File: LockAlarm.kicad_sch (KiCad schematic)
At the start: 6 parts, among them SW1 Reed Switch

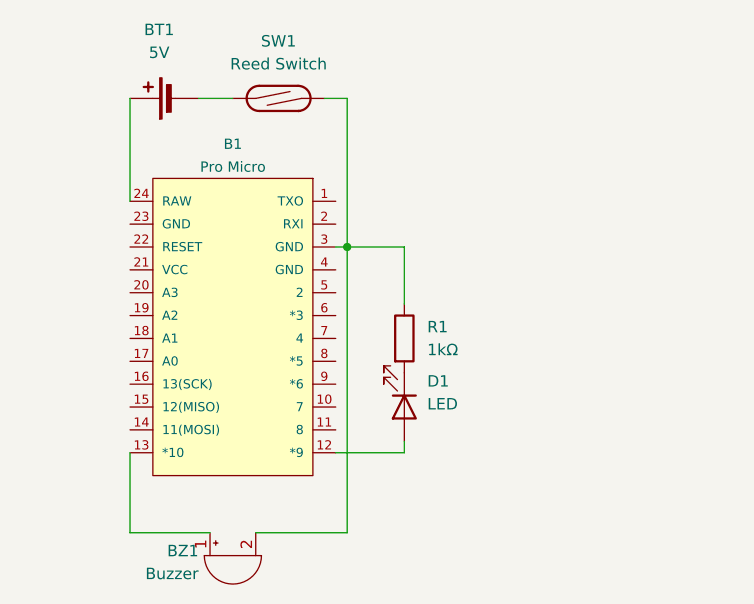
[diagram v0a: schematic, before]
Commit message: Replace ProMicro with ATtiny13A-P
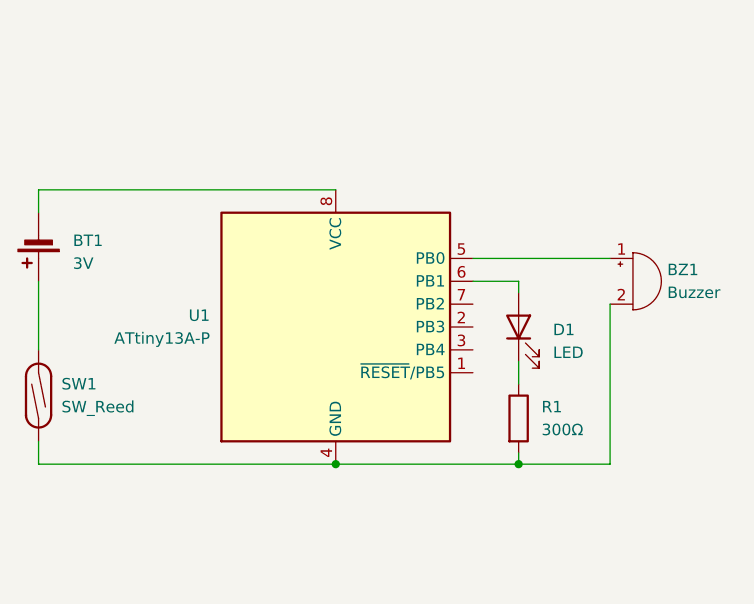
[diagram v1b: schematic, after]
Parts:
- removed B1: Pro Micro, SPARKFUN_PRO_MICRO, symbol SparkFun-Boards:SPARKFUN_PRO_MICRO
- added U1: ATtiny13A-P, Package_DIP:DIP-8_W7.62mm, symbol MCU_Microchip_ATtiny:ATtiny13A-P
- BT1: value 5V -> 3V
- R1: value 1kΩ -> 300Ω
- SW1: value Reed Switch -> SW_Reed
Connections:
- net at BT1.1 (+): now also SW1.1
- net at BT1.2 (-): now also U1.8 (VCC); no longer SW1.1
- net at BZ1.1 (-): now also U1.5 (PB0)
- net at BZ1.2 (+), SW1.2: now also R1.2, U1.4 (GND); no longer R1.1
- net at D1.1 (K): now also R1.1; no longer R1.2
- net at D1.2 (A): now also U1.6 (PB1)
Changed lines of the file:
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@@
 (kicad_sch (version 20230121) (generator eeschema)
   (paper "A5")
-  (junction (at 110.49 52.07) (diameter 0) (color 0 0 0 0)
+  (junction (at 109.22 76.2) (diameter 0) (color 0 0 0 0)
   )
-  (wire (pts (xy 86.36 83.82) (xy 95.25 83.82))
+  (junction (at 129.54 76.2) (diameter 0) (color 0 0 0 0)
+  )
+  (wire (pts (xy 129.54 76.2) (xy 139.7 76.2))
     (stroke (width 0) (type default))
   )
-  (wire (pts (xy 100.33 83.82) (xy 110.49 83.82))
+  (wire (pts (xy 124.46 53.34) (xy 139.7 53.34))
     (stroke (width 0) (type default))
   )
-  (wire (pts (xy 110.49 52.07) (xy 116.84 52.07))
+  (wire (pts (xy 76.2 45.72) (xy 76.2 48.26))
     (stroke (width 0) (type default))
   )
-  (wire (pts (xy 86.36 74.93) (xy 86.36 83.82))
+  (wire (pts (xy 129.54 55.88) (xy 124.46 55.88))
     (stroke (width 0) (type default))
   )
-  (wire (pts (xy 109.22 52.07) (xy 110.49 52.07))
+  (wire (pts (xy 109.22 76.2) (xy 129.54 76.2))
     (stroke (width 0) (type default))
   )
-  (wire (pts (xy 116.84 74.93) (xy 109.22 74.93))
+  (wire (pts (xy 129.54 67.31) (xy 129.54 64.77))
     (stroke (width 0) (type default))
   )
-  (wire (pts (xy 110.49 35.56) (xy 107.95 35.56))
+  (wire (pts (xy 109.22 45.72) (xy 76.2 45.72))
     (stroke (width 0) (type default))
   )
-  (wire (pts (xy 116.84 74.93) (xy 116.84 73.66))
+  (wire (pts (xy 76.2 76.2) (xy 109.22 76.2))
     (stroke (width 0) (type default))
   )
-  (wire (pts (xy 116.84 58.42) (xy 116.84 52.07))
+  (wire (pts (xy 129.54 57.15) (xy 129.54 55.88))
     (stroke (width 0) (type default))
   )
-  (wire (pts (xy 93.98 35.56) (xy 97.79 35.56))
+  (wire (pts (xy 139.7 58.42) (xy 139.7 76.2))
     (stroke (width 0) (type default))
   )
-  (wire (pts (xy 110.49 83.82) (xy 110.49 52.07))
+  (wire (pts (xy 129.54 74.93) (xy 129.54 76.2))
     (stroke (width 0) (type default))
   )
-  (wire (pts (xy 86.36 46.99) (xy 86.36 35.56))
+  (wire (pts (xy 76.2 73.66) (xy 76.2 76.2))
     (stroke (width 0) (type default))
   )
-  (wire (pts (xy 110.49 35.56) (xy 110.49 52.07))
+  (wire (pts (xy 76.2 55.88) (xy 76.2 63.5))
     (stroke (width 0) (type default))
   )
-  (symbol (lib_id "Device:Battery_Cell") (at 91.44 35.56 90) (unit 1)
+  (symbol (lib_id "Device:Buzzer") (at 142.24 55.88 0) (unit 1)
     (in_bom yes) (on_board yes) (dnp no) (fields_autoplaced)
-    (property "Reference" "BT1" (at 89.5985 27.94 90)
-      (effects (font (size 1.27 1.27)))
+    (property "Reference" "BZ1" (at 146.05 54.61 0)
+      (effects (font (size 1.27 1.27)) (justify left))
     )
-    (property "Value" "5V" (at 89.5985 30.48 90)
-      (effects (font (size 1.27 1.27)))
+    (property "Value" "Buzzer" (at 146.05 57.15 0)
+      (effects (font (size 1.27 1.27)) (justify left))
     )
-    (property "Footprint" "" (at 89.916 35.56 90)
+    (property "Footprint" "" (at 141.605 53.34 90)
       (effects (font (size 1.27 1.27)) hide)
     )
-    (property "Datasheet" "~" (at 89.916 35.56 90)
+    (property "Datasheet" "~" (at 141.605 53.34 90)
+      (effects (font (size 1.27 1.27)) hide)
+    )
+    (pin "1")
+    (pin "2")
+    (instances
+      (project "LockAlarm"
+        (path "/bfb8881f-b332-475f-bf27-97a988c7f65e"
+          (reference "BZ1") (unit 1)
+        )
+      )
+    )
+  )
+  (symbol (lib_id "Device:Battery_Cell") (at 76.2 50.8 180) (unit 1)
+    (in_bom yes) (on_board yes) (dnp no) (fields_autoplaced)
+    (property "Reference" "BT1" (at 80.01 51.3715 0)
+      (effects (font (size 1.27 1.27)) (justify right))
+    )
+    (property "Value" "3V" (at 80.01 53.9115 0)
+      (effects (font (size 1.27 1.27)) (justify right))
+    )
+    (property "Footprint" "" (at 76.2 52.324 90)
+      (effects (font (size 1.27 1.27)) hide)
+    )
+    (property "Datasheet" "~" (at 76.2 52.324 90)
       (effects (font (size 1.27 1.27)) hide)
     )
@@
     )
   )
-  (symbol (lib_id "Device:Buzzer") (at 97.79 86.36 90) (mirror x) (unit 1)
-    (in_bom yes) (on_board yes) (dnp no)
-    (property "Reference" "BZ1" (at 93.98 85.8451 90)
+  (symbol (lib_id "Switch:SW_Reed") (at 76.2 68.58 270) (unit 1)
+    (in_bom yes) (on_board yes) (dnp no) (fields_autoplaced)
+    (property "Reference" "SW1" (at 78.74 67.31 90)
       (effects (font (size 1.27 1.27)) (justify left))
     )
-    (property "Value" "Buzzer" (at 93.98 88.3851 90)
+    (property "Value" "SW_Reed" (at 78.74 69.85 90)
       (effects (font (size 1.27 1.27)) (justify left))
     )
-    (property "Footprint" "" (at 95.25 85.725 90)
+    (property "Footprint" "" (at 76.2 68.58 0)
       (effects (font (size 1.27 1.27)) hide)
     )
-    (property "Datasheet" "~" (at 95.25 85.725 90)
+    (property "Datasheet" "~" (at 76.2 68.58 0)
       (effects (font (size 1.27 1.27)) hide)
     )
@@
       (project "LockAlarm"
         (path "/bfb8881f-b332-475f-bf27-97a988c7f65e"
-          (reference "BZ1") (unit 1)
+          (reference "SW1") (unit 1)
         )
       )
     )
   )
-  (symbol (lib_id "Device:R") (at 116.84 62.23 0) (unit 1)
+  (symbol (lib_id "Device:LED") (at 129.54 60.96 90) (unit 1)
     (in_bom yes) (on_board yes) (dnp no) (fields_autoplaced)
-    (property "Reference" "R1" (at 119.38 60.96 0)
+    (property "Reference" "D1" (at 133.35 61.2775 90)
+      (effects (font (size 1.27 1.27)) (justify right))
+    )
+    (property "Value" "LED" (at 133.35 63.8175 90)
+      (effects (font (size 1.27 1.27)) (justify right))
+    )
+    (property "Footprint" "" (at 129.54 60.96 0)
+      (effects (font (size 1.27 1.27)) hide)
+    )
+    (property "Datasheet" "~" (at 129.54 60.96 0)
+      (effects (font (size 1.27 1.27)) hide)
+    )
+    (pin "1")
+    (pin "2")
+    (instances
+      (project "LockAlarm"
+        (path "/bfb8881f-b332-475f-bf27-97a988c7f65e"
+          (reference "D1") (unit 1)
+        )
+      )
+    )
+  )
+  (symbol (lib_id "Device:R") (at 129.54 71.12 0) (unit 1)
+    (in_bom yes) (on_board yes) (dnp no) (fields_autoplaced)
+    (property "Reference" "R1" (at 132.08 69.85 0)
       (effects (font (size 1.27 1.27)) (justify left))
     )
-    (property "Value" "1kΩ" (at 119.38 63.5 0)
+    (property "Value" "300Ω" (at 132.08 72.39 0)
       (effects (font (size 1.27 1.27)) (justify left))
     )
-    (property "Footprint" "" (at 115.062 62.23 90)
+    (property "Footprint" "" (at 127.762 71.12 90)
       (effects (font (size 1.27 1.27)) hide)
     )
-    (property "Datasheet" "~" (at 116.84 62.23 0)
+    (property "Datasheet" "~" (at 129.54 71.12 0)
       (effects (font (size 1.27 1.27)) hide)
     )
@@
     )
   )
-  (symbol (lib_id "Switch:SW_Reed") (at 102.87 35.56 0) (unit 1)
+  (symbol (lib_id "MCU_Microchip_ATtiny:ATtiny13A-P") (at 109.22 60.96 0) (unit 1)
     (in_bom yes) (on_board yes) (dnp no) (fields_autoplaced)
-    (property "Reference" "SW1" (at 102.87 29.21 0)
-      (effects (font (size 1.27 1.27)))
+    (property "Reference" "U1" (at 95.25 59.69 0)
+      (effects (font (size 1.27 1.27)) (justify right))
     )
-    (property "Value" "Reed Switch" (at 102.87 31.75 0)
-      (effects (font (size 1.27 1.27)))
+    (property "Value" "ATtiny13A-P" (at 95.25 62.23 0)
+      (effects (font (size 1.27 1.27)) (justify right))
     )
-    (property "Footprint" "" (at 102.87 35.56 0)
-      (effects (font (size 1.27 1.27)) hide)
+    (property "Footprint" "Package_DIP:DIP-8_W7.62mm" (at 109.22 60.96 0)
+      (effects (font (size 1.27 1.27) italic) hide)
     )
-    (property "Datasheet" "~" (at 102.87 35.56 0)
+    (property "Datasheet" "http://ww1.microchip.com/downloads/en/DeviceDoc/doc8126.pdf" (at 109.22 60.96 0)
       (effects (font (size 1.27 1.27)) hide)
     )
     (pin "1")
     (pin "2")
-    (instances
-      (project "LockAlarm"
-        (path "/bfb8881f-b332-475f-bf27-97a988c7f65e"
-          (reference "SW1") (unit 1)
-        )
-      )
-    )
-  )
-  (symbol (lib_id "SparkFun-Boards:SPARKFUN_PRO_MICRO") (at 97.79 60.96 0) (mirror y) (unit 1)
-    (in_bom yes) (on_board yes) (dnp no)
-    (property "Reference" "B1" (at 97.79 40.64 0)
-      (effects (font (size 1.143 1.143)))
-    )
-    (property "Value" "Pro Micro" (at 97.79 43.18 0)
-      (effects (font (size 1.143 1.143)))
-    )
-    (property "Footprint" "SPARKFUN_PRO_MICRO" (at 97.79 40.64 0)
-      (effects (font (size 0.508 0.508)) hide)
-    )
-    (property "Datasheet" "" (at 97.79 60.96 0)
-      (effects (font (size 1.27 1.27)) hide)
-    )
-    (pin "1")
-    (pin "10")
-    (pin "11")
-    (pin "12")
-    (pin "13")
-    (pin "14")
-    (pin "15")
-    (pin "16")
-    (pin "17")
-    (pin "18")
-    (pin "19")
-    (pin "2")
-    (pin "20")
-    (pin "21")
-    (pin "22")
-    (pin "23")
-    (pin "24")
     (pin "3")
     (pin "4")
@@
     (pin "7")
     (pin "8")
-    (pin "9")
     (instances
       (project "LockAlarm"
         (path "/bfb8881f-b332-475f-bf27-97a988c7f65e"
-          (reference "B1") (unit 1)
+          (reference "U1") (unit 1)
         )
       )
-    )
-  )
-  (symbol (lib_id "Device:LED") (at 116.84 69.85 270) (unit 1)
-    (in_bom yes) (on_board yes) (dnp no) (fields_autoplaced)
-    (property "Reference" "D1" (at 119.38 66.9925 90)
-      (effects (font (size 1.27 1.27)) (justify left))
-    )
-    (property "Value" "LED" (at 119.38 69.5325 90)
-      (effects (font (size 1.27 1.27)) (justify left))
-    )
-    (property "Footprint" "" (at 116.84 69.85 0)
-      (effects (font (size 1.27 1.27)) hide)
-    )
-    (property "Datasheet" "~" (at 116.84 69.85 0)
-      (effects (font (size 1.27 1.27)) hide)
-    )
-    (pin "1")
-    (pin "2")
-    (instances
-      (project "LockAlarm"
-        (path "/bfb8881f-b332-475f-bf27-97a988c7f65e"
-          (reference "D1") (unit 1)
-        )
-      )

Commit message: Fix schemaic
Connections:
- net at BT1.1 (+): now also U1.8 (VCC); no longer SW1.1
- net at BT1.2 (-): now also SW1.1; no longer U1.8 (VCC)
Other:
- moved on the sheet: BT1
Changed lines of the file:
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@@
   (junction (at 129.54 76.2) (diameter 0) (color 0 0 0 0)
+  )
+  (wire (pts (xy 76.2 55.88) (xy 76.2 63.5))
+    (stroke (width 0) (type default))
   )
   (wire (pts (xy 129.54 76.2) (xy 139.7 76.2))
@@
     (stroke (width 0) (type default))
   )
-  (wire (pts (xy 76.2 45.72) (xy 76.2 48.26))
+  (wire (pts (xy 76.2 45.72) (xy 109.22 45.72))
     (stroke (width 0) (type default))
   )
@@
   )
   (wire (pts (xy 129.54 67.31) (xy 129.54 64.77))
-    (stroke (width 0) (type default))
-  )
-  (wire (pts (xy 109.22 45.72) (xy 76.2 45.72))
     (stroke (width 0) (type default))
   )
@@
     (stroke (width 0) (type default))
   )
-  (wire (pts (xy 76.2 73.66) (xy 76.2 76.2))
+  (wire (pts (xy 76.2 48.26) (xy 76.2 45.72))
     (stroke (width 0) (type default))
   )
-  (wire (pts (xy 76.2 55.88) (xy 76.2 63.5))
+  (wire (pts (xy 76.2 73.66) (xy 76.2 76.2))
     (stroke (width 0) (type default))
   )
@@
     )
   )
-  (symbol (lib_id "Device:Battery_Cell") (at 76.2 50.8 180) (unit 1)
+  (symbol (lib_id "Device:Battery_Cell") (at 76.2 53.34 0) (unit 1)
     (in_bom yes) (on_board yes) (dnp no) (fields_autoplaced)
-    (property "Reference" "BT1" (at 80.01 51.3715 0)
-      (effects (font (size 1.27 1.27)) (justify right))
+    (property "Reference" "BT1" (at 80.01 50.2285 0)
+      (effects (font (size 1.27 1.27)) (justify left))
     )
-    (property "Value" "3V" (at 80.01 53.9115 0)
-      (effects (font (size 1.27 1.27)) (justify right))
+    (property "Value" "3V" (at 80.01 52.7685 0)
+      (effects (font (size 1.27 1.27)) (justify left))
     )
-    (property "Footprint" "" (at 76.2 52.324 90)
+    (property "Footprint" "" (at 76.2 51.816 90)
       (effects (font (size 1.27 1.27)) hide)
     )
-    (property "Datasheet" "~" (at 76.2 52.324 90)
+    (property "Datasheet" "~" (at 76.2 51.816 90)
       (effects (font (size 1.27 1.27)) hide)
     )
